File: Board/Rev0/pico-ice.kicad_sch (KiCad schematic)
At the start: 102 parts, among them J1 Connector_USB_B_Micro, J2 SPARE, J3 PMOD_PICO, J4 Dual PMOD A, J5 Conn_ARM_JTAG_SWD_10, J6 Single PMOD, J7 SPARES, J8 Dual PMOD B, J9 BOOT_SEL, SW1 ~{RESET}, SW2 SW_Push, U1 NCP1117ST33T3G, U2 W25Q32JVSSIQ, U3 RP2040, U4 AP2127K-1.2, U5 APS6404L-3SQN, U6 ICE40UP5K-SG48ITR, U8 W25Q32JVSSIQ, Y1 ABLS-12.000MHZ-B4-T

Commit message: Added MPN and footprint.
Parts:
- C1, C2: MPN (none) -> GCM1555C1H270JA16D; Manufacturer (none) -> Murata Electronics; Supplier (none) -> LCSC
- C10, C12, C14, C15, C16, C17, C18, C19, C20, C23, C24, C26, C27, C28, C29, C33, C35, C38, C39, C4, C40, C41, C42, C5, C8: footprint Capacitor_SMD:C_0603_1608Metric -> Capacitor_SMD:C_0402_1005Metric; MPN (none) -> GRM155R71C104KA88J; Manufacturer (none) -> Murata Electronics; Supplier (none) -> Mouser
- C11, C6: MPN (none) -> EMK105BJ105KV-F; Manufacturer (none) -> Taiyo Yuden; Supplier (none) -> LCSC
- C13, C22, C25, C3, C30, C31, C32, C34, C43, C7, C9: footprint Capacitor_SMD:C_0603_1608Metric -> Capacitor_SMD:C_0402_1005Metric; MPN (none) -> GRM155R60J475ME87D; Manufacturer (none) -> Murata Electronics; Supplier (none) -> LCSC
- C21: footprint Capacitor_SMD:C_0603_1608Metric -> Capacitor_SMD:C_0402_1005Metric; MPN C1005X5R0J104K050BA -> GRM155R71C104KA88J; Manufacturer (none) -> Murata Electronics; Supplier (none) -> Mouser
- D1: MPN (none) -> 1N4148WT-7; Manufacturer (none) -> Micro Commercial Co; Supplier (none) -> LCSC
- D2, D4: footprint VS.preety:LED_Cree-PLCC4_2x2mm_CW -> CUSTOM:LED_Cree-PLCC4_1x1mm_CW; Digi-Key Part Number (none) -> LCSC; MPN (none) -> MHPA1010RGBDT; Manufacturer (none) -> MEIHUA; Supplier (none) -> LCSC
- D3: MPN (none) -> LTST-C191KGKT; Manufacturer (none) -> Lite-On; Supplier (none) -> LCSC
- FID1, FID2, FID3, FID4, FID5, FID6, H1, H2, H3, H4, TP1: MPN (none) -> DNP
- J1: footprint (none) -> CUSTOM:MOLEX_47589-0001; MPN (none) -> 475890001; Manufacturer (none) -> Molex; Supplier (none) -> LCSC
- J2: value SPARE -> 6X2 Female Header; footprint (none) -> CUSTOM:PMOD_2x06_P2.54mm_Horizontal; Comment (none) -> SPARE; MPN (none) -> DW254W-22-12-85; Manufacturer (none) -> DEALON; Supplier (none) -> LCSC
- J3: value PMOD_PICO -> 6X2 Female Header; footprint (none) -> CUSTOM:PMOD_2x06_P2.54mm_Horizontal; Comment (none) -> PMOD_PICO; MPN (none) -> DW254W-22-12-85; Manufacturer (none) -> DEALON; Supplier (none) -> LCSC
- J4: value Dual PMOD A -> 6X2 Female Header; footprint (none) -> CUSTOM:PMOD_2x06_P2.54mm_Horizontal; Comment (none) -> Dual PMOD A; MPN (none) -> DW254W-22-12-85; Manufacturer (none) -> DEALON; Supplier (none) -> LCSC
- J5: footprint (none) -> Connector_PinHeader_1.27mm:PinHeader_2x05_P1.27mm_Vertical_SMD; MPN (none) -> PZ127VS-12-10-H10-A38; Manufacturer (none) -> XFCN; Supplier (none) -> LCSC
- J6: value Single PMOD -> 6X2 Female Header; footprint (none) -> CUSTOM:PMOD_2x06_P2.54mm_Horizontal; Comment (none) -> Single PMOD; MPN (none) -> DW254W-22-12-85; Manufacturer (none) -> DEALON; Supplier (none) -> LCSC
- J7: value SPARES -> 6X2 Female Header; footprint (none) -> CUSTOM:PMOD_2x06_P2.54mm_Horizontal; Comment (none) -> SPARES; MPN (none) -> DW254W-22-12-85; Manufacturer (none) -> DEALON; Supplier (none) -> LCSC
- J8: value Dual PMOD B -> 6X2 Female Header; footprint (none) -> CUSTOM:PMOD_2x06_P2.54mm_Horizontal; Comment (none) -> Dual PMOD B; MPN (none) -> DW254W-22-12-85; Manufacturer (none) -> DEALON; Supplier (none) -> LCSC
- J9: footprint (none) -> Connector_PinHeader_2.54mm:PinHeader_1x02_P2.54mm_Vertical; MPN (none) -> PZ254V-11-02P; Manufacturer (none) -> XFCN; Supplier (none) -> LCSC
- PTC1: MPN (none) -> MF-FSMF035X-2; Manufacturer (none) -> Bourns Inc.; Supplier (none) -> LCSC
- R1, R2: footprint Capacitor_SMD:C_0402_1005Metric -> Resistor_SMD:R_0402_1005Metric; MPN (none) -> RC0402FR-071KL; Manufacturer (none) -> YAGEO; Supplier (none) -> LCSC
- R11: footprint Resistor_SMD:R_0603_1608Metric -> Resistor_SMD:R_0402_1005Metric; MPN (none) -> RC0402FR-07100RL; Manufacturer (none) -> YAGEO; Supplier (none) -> LCSC
- R12, R13, R15, R16, R17, R21, R7, R8, R9: footprint Resistor_SMD:R_0603_1608Metric -> Resistor_SMD:R_0402_1005Metric; MPN (none) -> RC0402FR-0710KL; Manufacturer (none) -> YAGEO; Supplier (none) -> LCSC
- R14, R18, R19, R20: footprint Resistor_SMD:R_0603_1608Metric -> Resistor_SMD:R_0402_1005Metric; MPN (none) -> RC0402FR-072K2L; Manufacturer (none) -> YAGEO; Supplier (none) -> LCSC
- R22, R23, R4, R5, R6: footprint Capacitor_SMD:C_0402_1005Metric -> Resistor_SMD:R_0402_1005Metric; MPN (none) -> RC0402FR-0727RL; Manufacturer (none) -> YAGEO; Supplier (none) -> LCSC
- R3: value DNF -> DNP; footprint Capacitor_SMD:C_0402_1005Metric -> Resistor_SMD:R_0402_1005Metric; MPN (none) -> DNP
- SJ1: renamed from R10; footprint vs:ShortedJumper-2_P1.3mm_Bridged_Pad1.0x1.0mm -> Jumper:SolderJumper-2_P1.3mm_Bridged_RoundedPad1.0x1.5mm; MPN (none) -> DNP
- SJ4, SJ5: footprint vs:ShortedJumper-2_P1.3mm_Bridged_Pad1.0x1.0mm -> Jumper:SolderJumper-2_P1.3mm_Bridged_RoundedPad1.0x1.5mm; MPN (none) -> DNP
- SJ6: footprint vs:SolderJumper-2_0603_Open_TrianglePad1.0x1.5mm -> Jumper:SolderJumper-2_P1.3mm_Open_TrianglePad1.0x1.5mm; MPN (none) -> DNP
- SW1: value ~{RESET} -> PTS820 J25K SMTR LFS; footprint (none) -> CUSTOM:PTS820J25KSMTRLFS; Comment (none) -> ~RESET; MPN (none) -> PTS820 J25K SMTR LFS; Manufacturer (none) -> C&K; Supplier (none) -> Mouser
- SW2: value SW_Push -> PTS820 J25K SMTR LFS; footprint (none) -> CUSTOM:PTS820J25KSMTRLFS; Comment (none) -> SW_Push; MPN (none) -> PTS820 J25K SMTR LFS; Manufacturer (none) -> C&K; Supplier (none) -> Mouser
- U1: MPN (none) -> NCP1117ST33T3G; Manufacturer (none) -> onsemi; Supplier (none) -> LCSC
- U2, U8: MPN (none) -> W25Q32JVSSIQ; Manufacturer (none) -> Winbond Elec; Supplier (none) -> LCSC
- U3: MPN (none) -> RP2040; Manufacturer (none) -> Raspberry Pi; Supplier (none) -> LCSC
- U4: value AP2127K-1.2 -> CL9293A12L5M; footprint vs:SOT-23-5 -> Package_TO_SOT_SMD:SOT-23-5; MPN (none) -> CL9293A12L5M; Manufacturer (none) -> ChipLink Tech; Supplier (none) -> LCSC
- U5: value APS6404L-3SQN -> APS6404L-3SQN-SN; footprint Package_SO:SOIC-8_5.23x5.23mm_P1.27mm -> Package_SO:SOIC-8_3.9x4.9mm_P1.27mm; MPN (none) -> APS6404L-3SQN-SN; Manufacturer (none) -> AP Memory; Supplier (none) -> Mouser
- U6: MPN (none) -> ICE40UP5K-SG48I; Manufacturer (none) -> Lattice; Supplier (none) -> Mouser
- Y1: MPN (none) -> ABLS-12.000MHZ-B4-T; Manufacturer (none) -> Abracon LLC; Supplier (none) -> Mouser
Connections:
- net GND: now also J1.SH (Shield); no longer J1.6 (Shield)

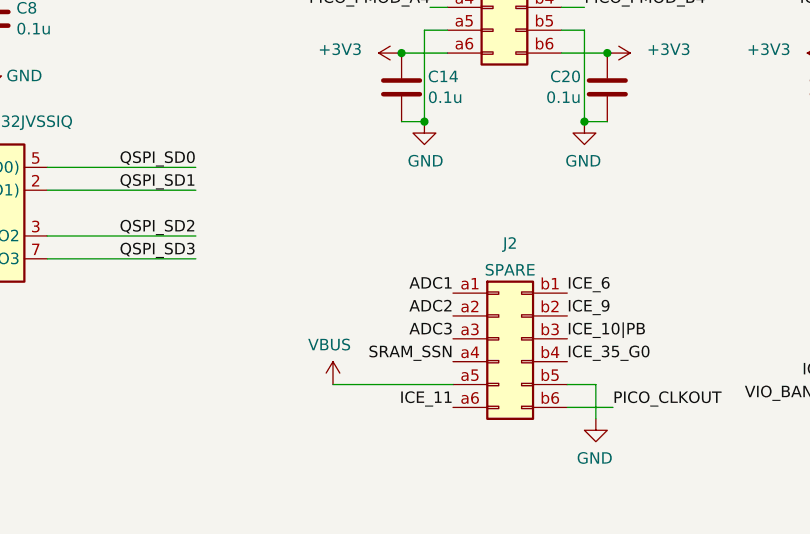
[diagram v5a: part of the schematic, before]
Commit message: Rough placement, needs work to compress this and center everything into 0.1" centers
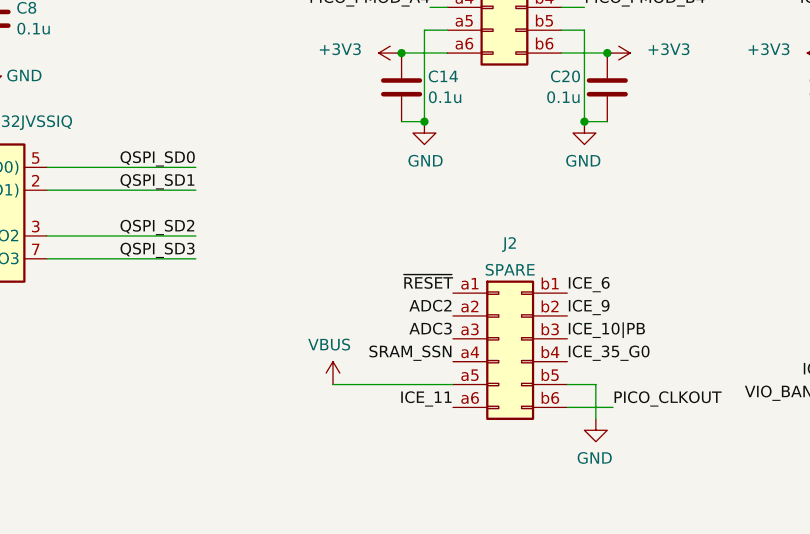
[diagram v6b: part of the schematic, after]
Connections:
- net ADC1 is gone; now on net ~{RESET}: J2.a1 (Pin_a1)
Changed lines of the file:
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@@
     (effects (font (size 1.27 1.27)) (justify left bottom))
+  )
+  (label "~{RESET}" (at 148.59 259.08 180)
+    (effects (font (size 1.27 1.27)) (justify right bottom))
   )
   (label "ICE_LED_R" (at 181.61 191.77 0)
@@
     (effects (font (size 1.27 1.27)) (justify left bottom))
   )
-  (label "ADC1" (at 148.59 259.08 180)
-    (effects (font (size 1.27 1.27)) (justify right bottom))
-  )
   (label "SRAM_SSN" (at 181.61 171.45 0)

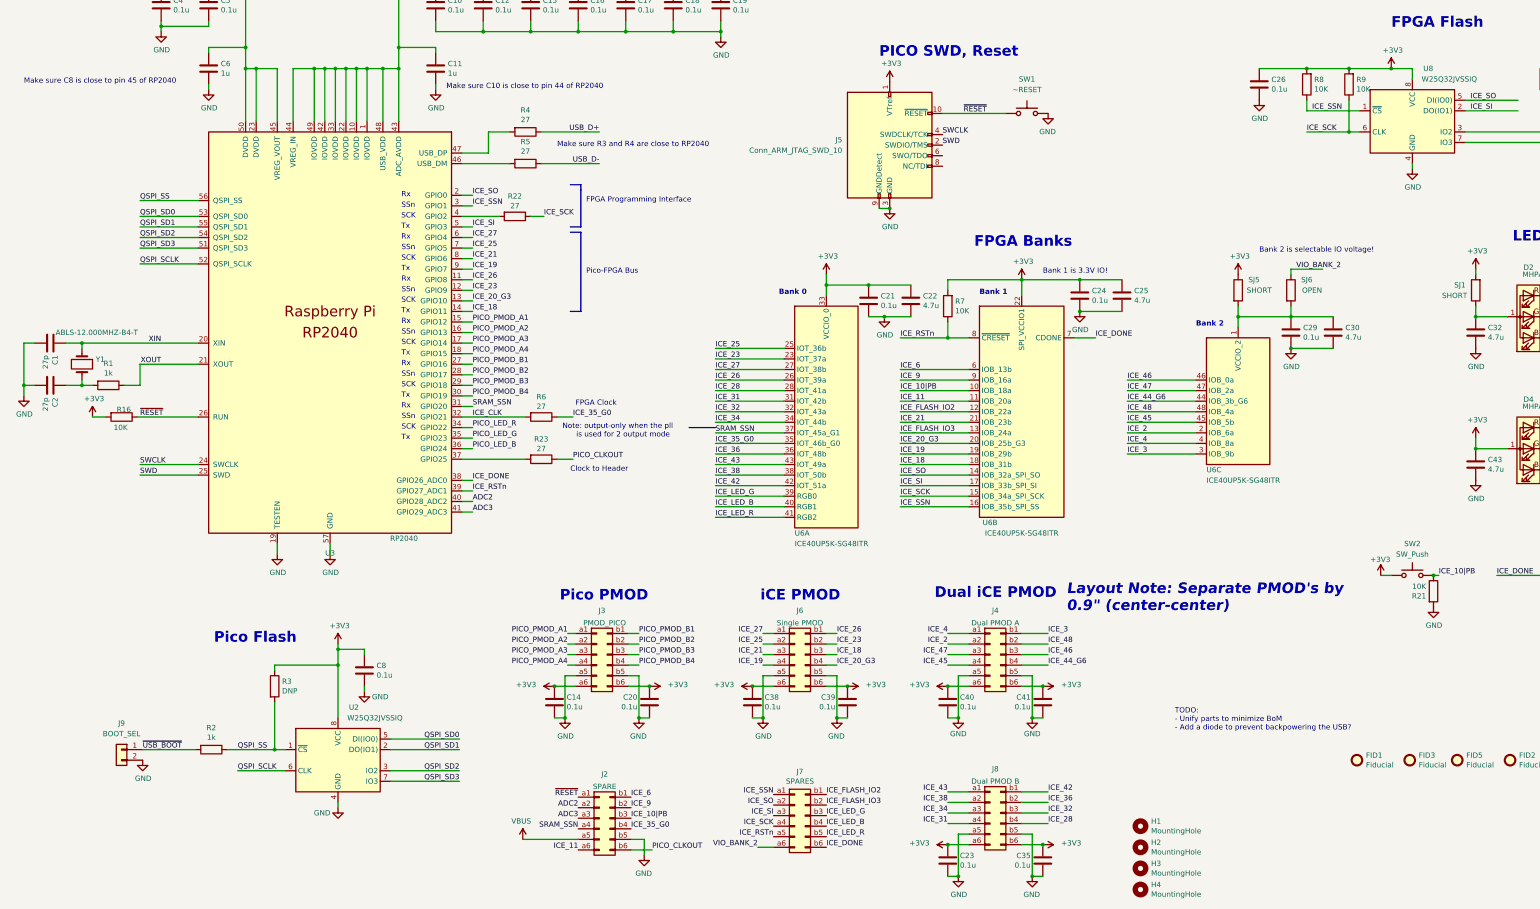
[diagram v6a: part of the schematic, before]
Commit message: Finished the preliminary placement.
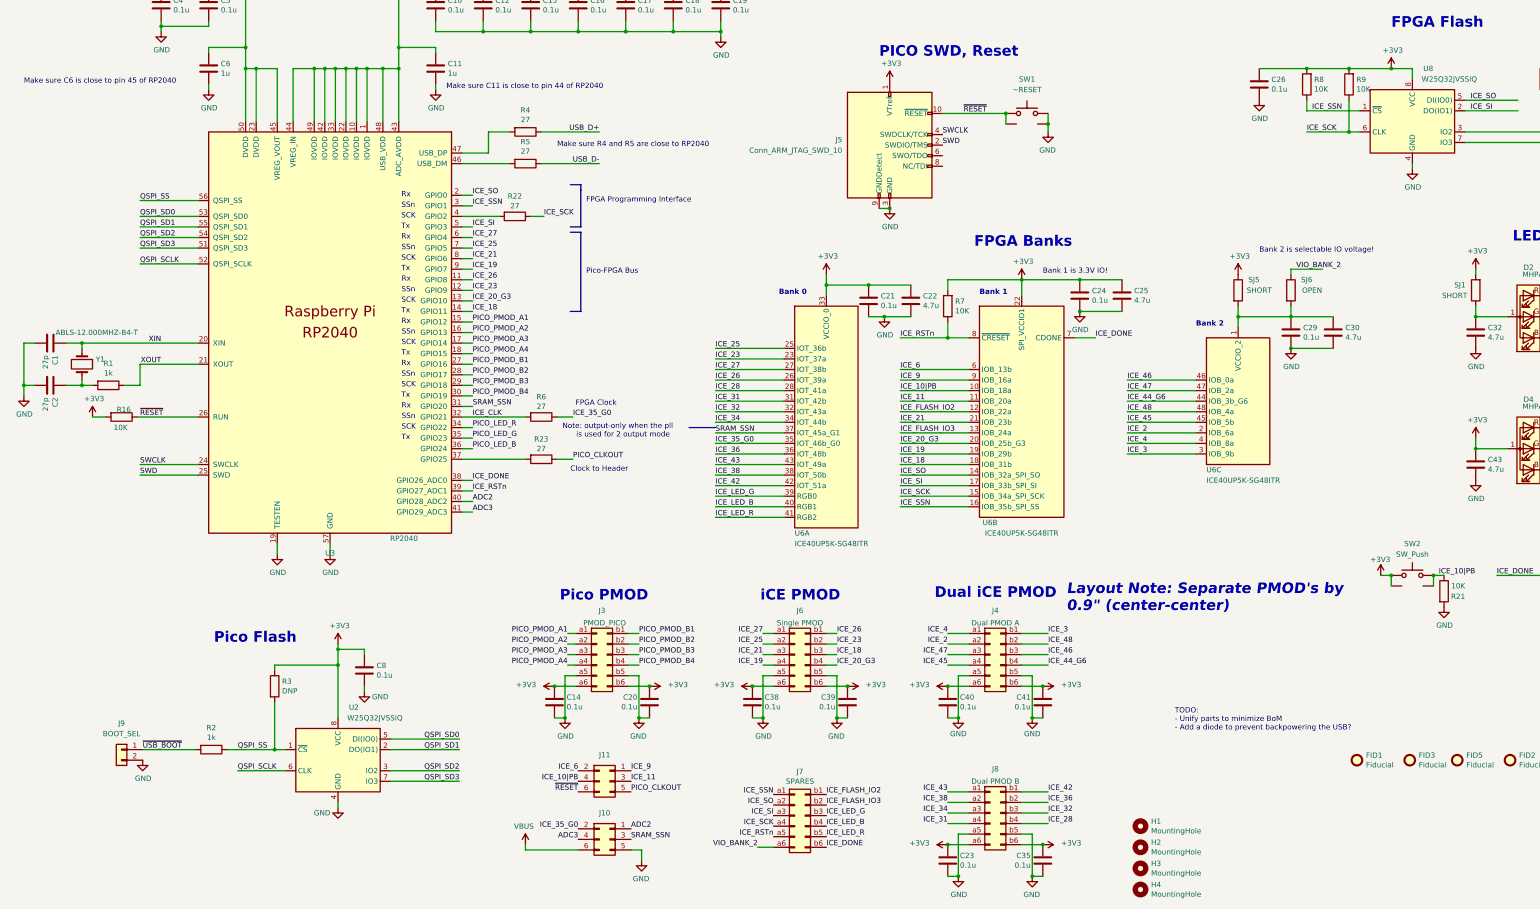
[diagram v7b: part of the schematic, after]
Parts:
- removed J2: 6X2 Female Header, CUSTOM:PMOD_2x06_P2.54mm_Horizontal, symbol Connector_Generic:Conn_02x06_Row_Letter_First
- added J10, J11: 2x3_2.54mm_Female, Connector_PinSocket_2.54mm:PinSocket_2x03_P2.54mm_Horizontal, symbol 2x3FemaleHeader:2x3_2.54mm_Female
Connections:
- net +3V3: now also SW2.SH1
- net ADC2: now also J10.1
- net ADC3: now also J10.4
- net GND: now also SW1.SH1, J10.5
- net ICE_10|PB: now also SW2.SH2, J11.4
- net ICE_11: now also J11.3
- net ICE_35_G0: now also J10.2
- net ICE_6: now also J11.2
- net ICE_9: now also J11.1
- net PICO_CLKOUT: now also J11.5
- net SRAM_SSN: now also J10.3
- net VBUS: now also J10.6
- net ~{RESET}: now also SW1.SH2, J11.6
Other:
- note added: "Make sure C11 is close to pin 44 of RP2040"
- note added: "Make sure C6 is close to pin 45 of RP2040"
- note added: "Make sure R4 and R5 are close to RP2040"
- note removed: "Make sure C10 is close to pin 44 of RP2040"
- note removed: "Make sure C8 is close to pin 45 of RP2040"
- note removed: "Make sure R3 and R4 are close to RP2040"
- moved on the sheet: R21

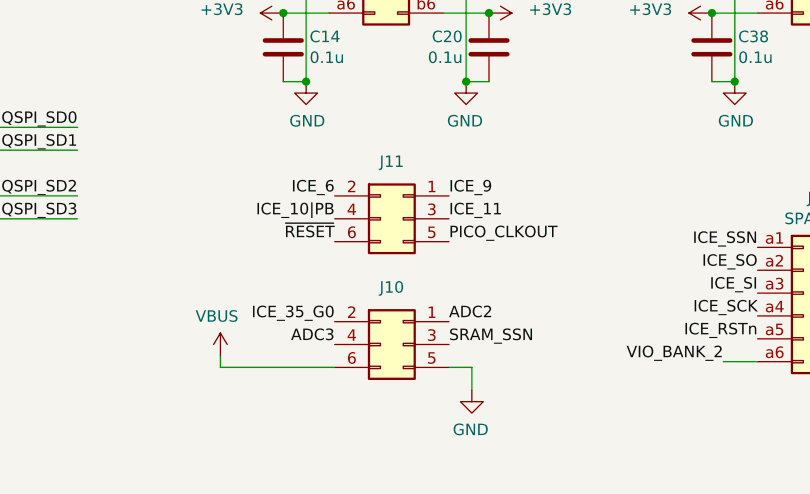
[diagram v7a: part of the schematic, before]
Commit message: Minor net reallocation
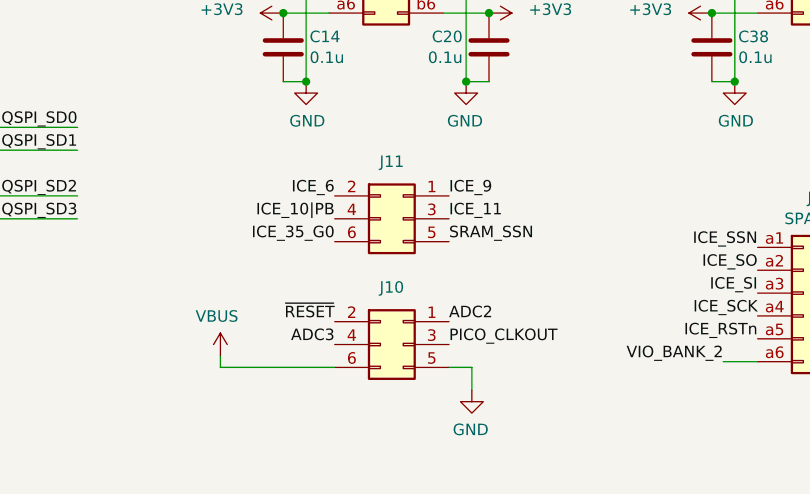
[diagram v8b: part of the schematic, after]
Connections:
- net ICE_35_G0: now also J11.6; no longer J10.2
- net PICO_CLKOUT: now also J10.3; no longer J11.5
- net SRAM_SSN: now also J11.5; no longer J10.3
- net ~{RESET}: now also J10.2; no longer J11.6
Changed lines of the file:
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@@
     (effects (font (size 1.27 1.27)) (justify left bottom))
-  )
-  (label "~{RESET}" (at 148.59 257.81 180)
-    (effects (font (size 1.27 1.27)) (justify right bottom))
   )
   (label "ICE_LED_R" (at 181.61 191.77 0)
@@
     (effects (font (size 1.27 1.27)) (justify left bottom))
   )
+  (label "SRAM_SSN" (at 161.29 257.81 0)
+    (effects (font (size 1.27 1.27)) (justify left bottom))
+  )
   (label "ICE_SI" (at 373.38 45.72 0)
     (effects (font (size 1.27 1.27)) (justify left bottom))
@@
     (effects (font (size 1.27 1.27)) (justify right bottom))
   )
+  (label "ICE_35_G0" (at 148.59 257.81 180)
+    (effects (font (size 1.27 1.27)) (justify right bottom))
+  )
   (label "ICE_2" (at 237.49 222.25 180)
     (effects (font (size 1.27 1.27)) (justify right bottom))
@@
     (effects (font (size 1.27 1.27)) (justify left bottom))
   )
-  (label "SRAM_SSN" (at 161.29 269.24 0)
-    (effects (font (size 1.27 1.27)) (justify left bottom))
-  )
   (label "ICE_46" (at 280.67 158.75 0)
     (effects (font (size 1.27 1.27)) (justify left bottom))
@@
     (effects (font (size 1.27 1.27)) (justify right bottom))
   )
+  (label "PICO_CLKOUT" (at 161.29 269.24 0)
+    (effects (font (size 1.27 1.27)) (justify left bottom))
+  )
   (label "ICE_4" (at 280.67 173.99 0)
     (effects (font (size 1.27 1.27)) (justify left bottom))
@@
     (effects (font (size 1.27 1.27)) (justify left bottom))
   )
-  (label "PICO_CLKOUT" (at 161.29 257.81 0)
-    (effects (font (size 1.27 1.27)) (justify left bottom))
-  )
   (label "VCC_PLL" (at 295.91 31.75 0)
     (effects (font (size 1.27 1.27)) (justify left bottom))
@@
     (effects (font (size 1.27 1.27)) (justify left bottom))
   )
-  (label "ICE_35_G0" (at 148.59 266.7 180)
-    (effects (font (size 1.27 1.27)) (justify right bottom))
-  )
   (label "ICE_42" (at 181.61 184.15 0)
     (effects (font (size 1.27 1.27)) (justify left bottom))
@@
     (effects (font (size 1.27 1.27)) (justify left bottom))
   )
+  (label "~{RESET}" (at 148.59 266.7 180)
+    (effects (font (size 1.27 1.27)) (justify right bottom))
+  )
   (label "ICE_6" (at 226.06 156.21 0)
